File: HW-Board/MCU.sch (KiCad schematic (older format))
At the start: 22 parts

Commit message: sync
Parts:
- added C23, C24: 100n, symbol Device:C_Small
- added C25: 100n, symbol Device:C
- added J3: UART, symbol Connector:Conn_01x04_Male
- added R6, R7, R8: R, symbol Device:R
- added ROT1: ROTARY-ENCODER-Ebay, symbol Peters:ROTARY-ENCODER-Ebay
- added U8: SN74LVC2G14, TO_SOT_Packages_SMD:SOT-23-6_Handsoldering, symbol Peters:SN74LVC2G14
- gave numbers to parts that had none: 22
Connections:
- net +3V3: now also C25.1, R6.1, R7.1, R8.1, U8.5 (VCC)
- net GND: now also C23.2, C24.2, C25.2, J3.4 (Pin_4), ROT1.2 (C), ROT1.4 (SW2), U8.2 (GND)
- net RX: now also J3.3 (Pin_3)
- net TX: now also J3.2 (Pin_2)
- net encA: now reaches U6.15 (PB10_SCL2_TX3_5V)
- net encA: now also U8.6 (Y)
- net encSW: now reaches U6.16 (PB11_SDA2_RX3_5V)
- net encSW: now also R6.2, ROT1.5 (SW1)
- net NegativeSet1 renamed encB
- net encB: now also U8.4 (Y)
- net NegativeSet2: no longer names the net of U6.13 (PB0_ADC8_PWM)
- new net: C24.1, R7.2, ROT1.1 (A), U8.1 (A)
- new net: C23.1, R8.2, ROT1.3 (B), U8.3 (A)
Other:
- moved on the sheet: D2A, D3A, R_I2CPullUp1, R_I2CPullUp2

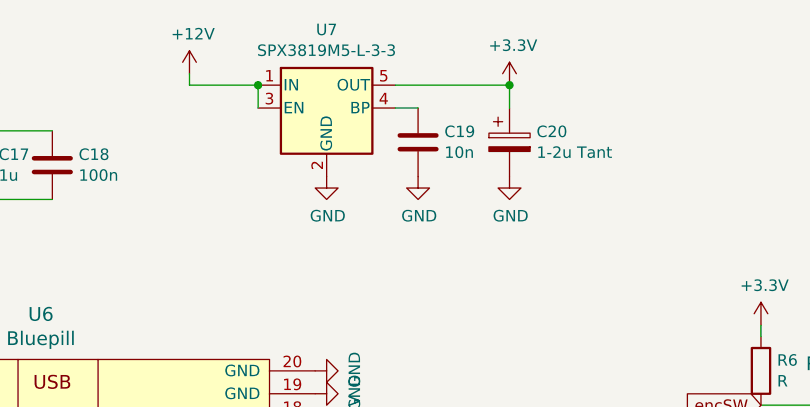
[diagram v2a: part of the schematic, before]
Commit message: 5v isolation and better opamps
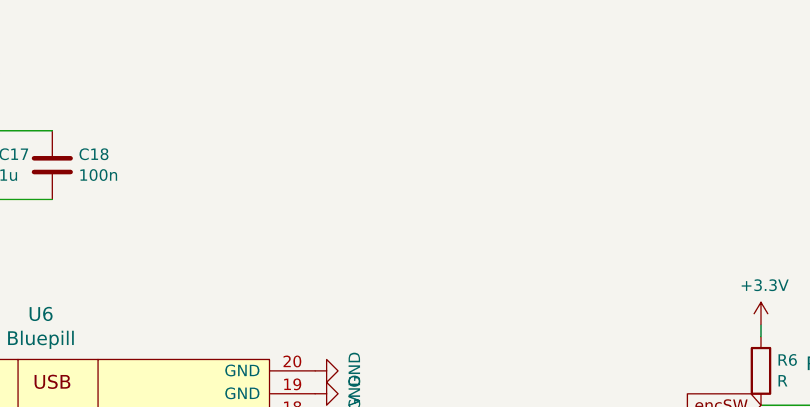
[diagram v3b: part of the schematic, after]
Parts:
- removed C19: 10n, symbol Device:C
- removed C20: 1-2u Tant, symbol Device:CP
- removed U7: SPX3819M5-L-3-3, Package_TO_SOT_SMD:SOT-23-5, symbol Regulator_Linear:SPX3819M5-L-3-3
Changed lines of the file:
@@
-$EndComp
-$Comp
-L Regulator_Linear:SPX3819M5-L-3-3 U7
-U 1 1 5D4D1C8C
-P 5100 1200
-F 0 "U7" H 5100 1542 50  0000 C CNN
-F 1 "SPX3819M5-L-3-3" H 5100 1451 50  0000 C CNN
-F 2 "Package_TO_SOT_SMD:SOT-23-5" H 5100 1525 50  0001 C CNN
-F 3 "https://www.exar.com/content/document.ashx?id=22106&languageid=1033&type=Datasheet&partnumber=SPX3819&filename=SPX3819.pdf&part=SPX3819" H 5100 1200 50  0001 C CNN
-	1    5100 1200
-	1    0    0    -1
-$EndComp
-$Comp
-L power:+12V #PWR0160
-U 1 1 5D4D49AD
-P 4500 1050
-F 0 "#PWR0160" H 4500 900 50  0001 C CNN
-F 1 "+12V" H 4515 1223 50  0000 C CNN
-F 2 "" H 4500 1050 50  0001 C CNN
-F 3 "" H 4500 1050 50  0001 C CNN
-	1    4500 1050
-	1    0    0    -1
-$EndComp
-Wire Wire Line
-	4800 1100 4500 1100
-Wire Wire Line
-	4500 1100 4500 1050
-$Comp
-L Device:C C?
-U 1 1 5D4D693C
-P 5500 1350
-AR Path="/5D4D693C" Ref="C?"  Part="1"
-AR Path="/5D42C521/5D4D693C" Ref="C19"  Part="1"
-F 0 "C19" H 5615 1396 50  0000 L CNN
-F 1 "10n" H 5615 1305 50  0000 L CNN
-F 2 "" H 5538 1200 50  0001 C CNN
-F 3 "~" H 5500 1350 50  0001 C CNN
-	1    5500 1350
-	1    0    0    -1
-$EndComp
-Wire Wire Line
-	5500 1200 5400 1200
-$Comp
-L power:+3.3V #PWR?
-U 1 1 5D4D890C
-P 5900 1100
-AR Path="/5D4D890C" Ref="#PWR?"  Part="1"
-AR Path="/5D42C521/5D4D890C" Ref="#PWR0162"  Part="1"
-F 0 "#PWR0162" H 5900 950 50  0001 C CNN
-F 1 "+3.3V" H 5915 1273 50  0000 C CNN
-F 2 "" H 5900 1100 50  0001 C CNN
-F 3 "" H 5900 1100 50  0001 C CNN
-	1    5900 1100
-	1    0    0    -1
-$EndComp
-Wire Wire Line
-	5400 1100 5900 1100
-Wire Wire Line
-	5900 1100 5900 1200
-Connection ~ 5900 1100
-Wire Wire Line
-	4800 1200 4800 1100
-Connection ~ 4800 1100
-$Comp
-L Device:CP C20
-U 1 1 5D4E21A7
-P 5900 1350
-F 0 "C20" H 6018 1396 50  0000 L CNN
-F 1 "1-2u Tant" H 6018 1305 50  0000 L CNN
-F 2 "" H 5938 1200 50  0001 C CNN
-F 3 "~" H 5900 1350 50  0001 C CNN
-	1    5900 1350
-	1    0    0    -1
 $EndComp
 $Comp
@@
 Text GLabel 1400 5900 2    50   Input ~ 0
 TX
-$Comp
-L power:GND #PWR?
-U 1 1 5D4DDDD2
-P 5900 1500
-AR Path="/5D4DDDD2" Ref="#PWR?"  Part="1"
-AR Path="/5D42C521/5D4DDDD2" Ref="#PWR0163"  Part="1"
-F 0 "#PWR0163" H 5900 1250 50  0001 C CNN
-F 1 "GND" H 5905 1327 50  0000 C CNN
-F 2 "" H 5900 1500 50  0001 C CNN
-F 3 "" H 5900 1500 50  0001 C CNN
-	1    5900 1500
-	1    0    0    -1
-$EndComp
-$Comp
-L power:GND #PWR?
-U 1 1 5D4D769E
-P 5500 1500
-AR Path="/5D4D769E" Ref="#PWR?"  Part="1"
-AR Path="/5D42C521/5D4D769E" Ref="#PWR0161"  Part="1"
-F 0 "#PWR0161" H 5500 1250 50  0001 C CNN
-F 1 "GND" H 5505 1327 50  0000 C CNN
-F 2 "" H 5500 1500 50  0001 C CNN
-F 3 "" H 5500 1500 50  0001 C CNN
-	1    5500 1500
-	1    0    0    -1
-$EndComp
-$Comp
-L power:GND #PWR?
-U 1 1 5D4D405D
-P 5100 1500
-AR Path="/5D4D405D" Ref="#PWR?"  Part="1"
-AR Path="/5D42C521/5D4D405D" Ref="#PWR0159"  Part="1"
-F 0 "#PWR0159" H 5100 1250 50  0001 C CNN
-F 1 "GND" H 5105 1327 50  0000 C CNN
-F 2 "" H 5100 1500 50  0001 C CNN
-F 3 "" H 5100 1500 50  0001 C CNN
-	1    5100 1500
-	1    0    0    -1
-$EndComp
 $EndSCHEMATC

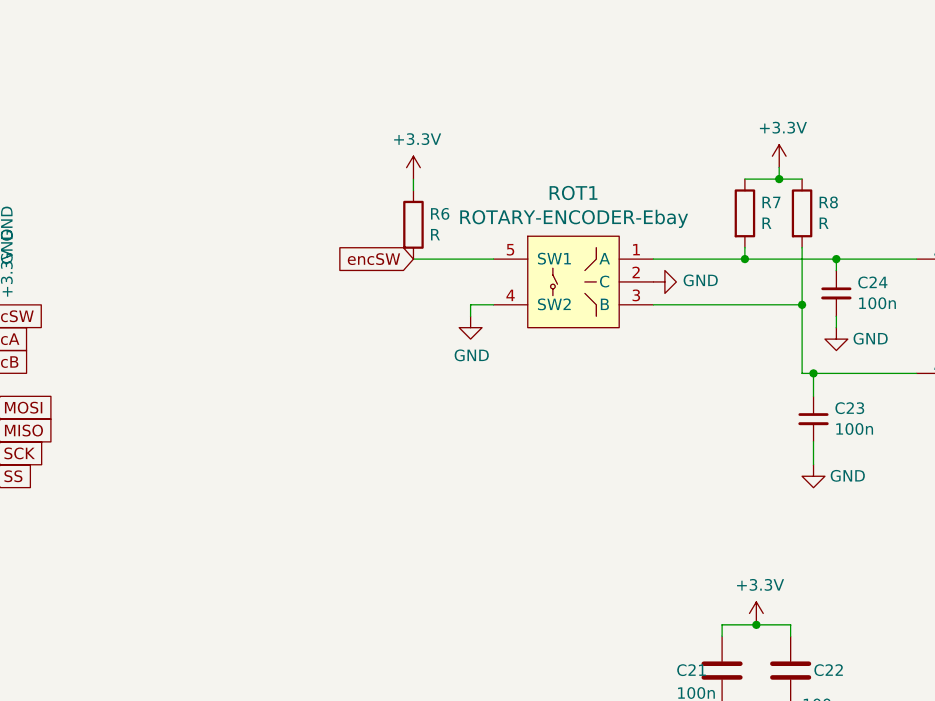
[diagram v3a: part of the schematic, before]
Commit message: added schmidt on encoder button
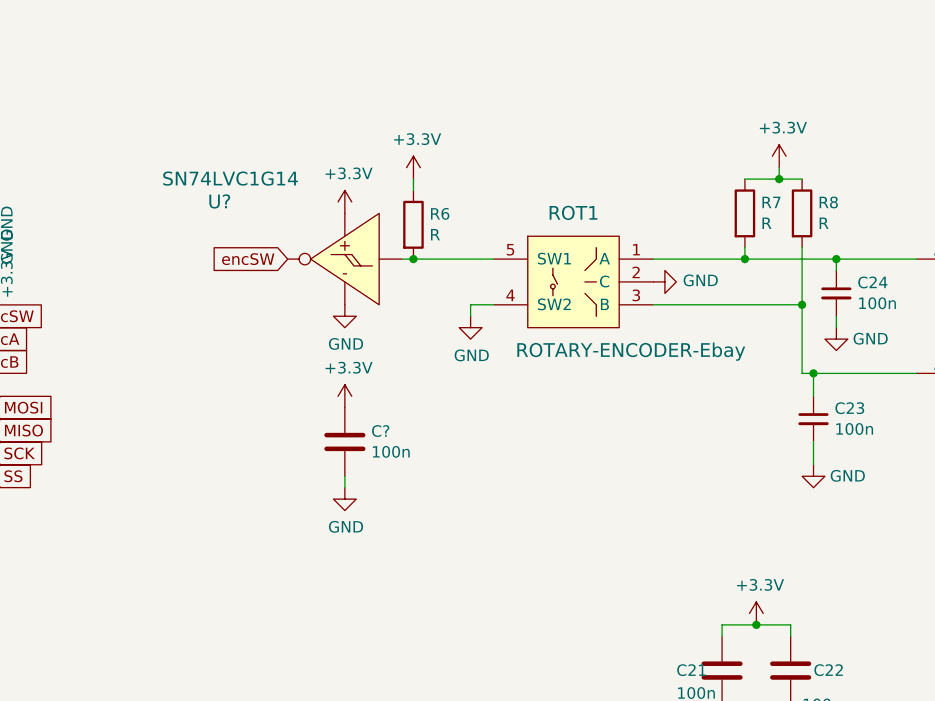
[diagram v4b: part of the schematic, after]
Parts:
- added C?: 100n, symbol Device:C
- added U?: SN74LVC1G14, TO_SOT_Packages_SMD:SOT-23-5_HandSoldering, symbol Peters:SN74LVC1G14
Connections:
- net +3V3: now also C?.1, U?.5 (VCC)
- net GND: now also C?.2, U?.3 (GND)
- net encSW: now also U?.4 (Y); no longer R6.2, ROT1.5 (SW1)
- new net: R6.2, ROT1.5 (SW1), U?.2 (A)
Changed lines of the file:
@@
 U 1 1 5D0958DD
 P 7700 2600
-F 0 "ROT1" H 7700 2987 60  0000 C CNN
-F 1 "ROTARY-ENCODER-Ebay" H 7700 2881 60  0000 C CNN
+F 0 "ROT1" H 7700 2900 60  0000 C CNN
+F 1 "ROTARY-ENCODER-Ebay" H 7950 2300 60  0000 C CNN
 F 2 "" H 7700 2600 60  0000 C CNN
 F 3 "" H 7700 2600 60  0000 C CNN
@@
 Text GLabel 9900 3000 2    50   Input ~ 0
 encB
-Text GLabel 7000 2500 0    50   Input ~ 0
+Text GLabel 6450 2500 0    50   Input ~ 0
 encSW
 Text GLabel 5050 2750 2    50   Input ~ 0
@@
 Text GLabel 1400 5900 2    50   Input ~ 0
 TX
+Wire Wire Line
+	7000 2500 6950 2500
+Connection ~ 7000 2500
+$Comp
+L Peters:SN74LVC1G14 U?
+U 1 1 5D50A9CE
+P 6700 2500
+F 0 "U?" H 7300 2750 60  0000 R CNN
+F 1 "SN74LVC1G14" H 7500 2850 60  0000 R CNN
+F 2 "TO_SOT_Packages_SMD:SOT-23-5_HandSoldering" H 6700 3250 60  0001 C CNN
+F 3 "" H 6700 3100 60  0001 C CNN
+	1    6700 2500
+	-1   0    0    -1
+$EndComp
+$Comp
+L power:+3.3V #PWR?
+U 1 1 5D523AB0
+P 6700 2300
+AR Path="/5D523AB0" Ref="#PWR?"  Part="1"
+AR Path="/5D42C521/5D523AB0" Ref="#PWR?"  Part="1"
+F 0 "#PWR?" H 6700 2150 50  0001 C CNN
+F 1 "+3.3V" H 6715 2473 50  0000 C CNN
+F 2 "" H 6700 2300 50  0001 C CNN
+F 3 "" H 6700 2300 50  0001 C CNN
+	1    6700 2300
+	1    0    0    -1
+$EndComp
+$Comp
+L power:GND #PWR?
+U 1 1 5D5241A7
+P 6700 2700
+F 0 "#PWR?" H 6700 2450 50  0001 C CNN
+F 1 "GND" H 6705 2527 50  0000 C CNN
+F 2 "" H 6700 2700 50  0001 C CNN
+F 3 "" H 6700 2700 50  0001 C CNN
+	1    6700 2700
+	1    0    0    -1
+$EndComp
+$Comp
+L Device:C C?
+U 1 1 5D524955
+P 6700 3300
+AR Path="/5D524955" Ref="C?"  Part="1"
+AR Path="/5D42C521/5D524955" Ref="C?"  Part="1"
+F 0 "C?" H 6815 3346 50  0000 L CNN
+F 1 "100n" H 6815 3255 50  0000 L CNN
+F 2 "" H 6738 3150 50  0001 C CNN
+F 3 "~" H 6700 3300 50  0001 C CNN
+	1    6700 3300
+	1    0    0    -1
+$EndComp
+$Comp
+L power:GND #PWR?
+U 1 1 5D52495F
+P 6700 3500
+AR Path="/5D52495F" Ref="#PWR?"  Part="1"
+AR Path="/5D42C521/5D52495F" Ref="#PWR?"  Part="1"
+F 0 "#PWR?" H 6700 3250 50  0001 C CNN
+F 1 "GND" H 6705 3327 50  0000 C CNN
+F 2 "" H 6700 3500 50  0001 C CNN
+F 3 "" H 6700 3500 50  0001 C CNN
+	1    6700 3500
+	1    0    0    -1
+$EndComp
+Wire Wire Line
+	6700 3450 6700 3500
+$Comp
+L power:+3.3V #PWR?
+U 1 1 5D52496A
+P 6700 3150
+AR Path="/5D52496A" Ref="#PWR?"  Part="1"
+AR Path="/5D42C521/5D52496A" Ref="#PWR?"  Part="1"
+F 0 "#PWR?" H 6700 3000 50  0001 C CNN
+F 1 "+3.3V" H 6715 3323 50  0000 C CNN
+F 2 "" H 6700 3150 50  0001 C CNN
+F 3 "" H 6700 3150 50  0001 C CNN
+	1    6700 3150
+	1    0    0    -1
+$EndComp
 $EndSCHEMATC

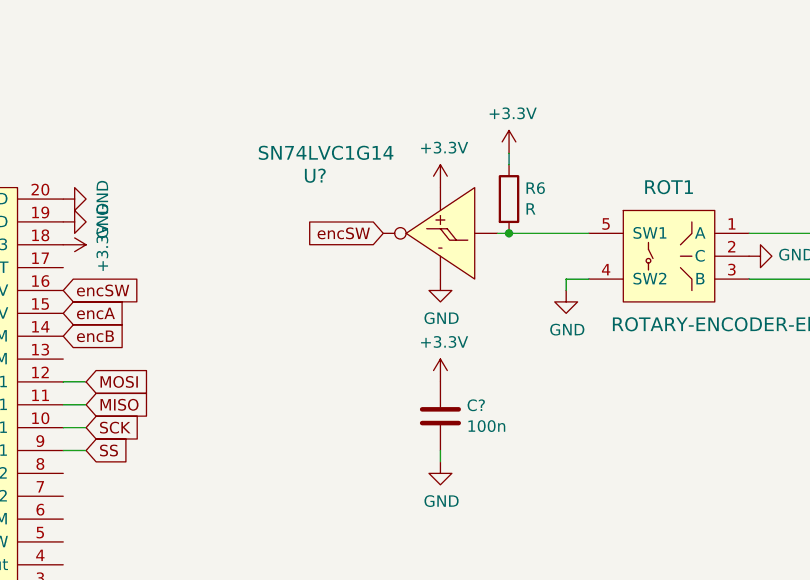
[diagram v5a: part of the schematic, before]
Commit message: Negative regulation done
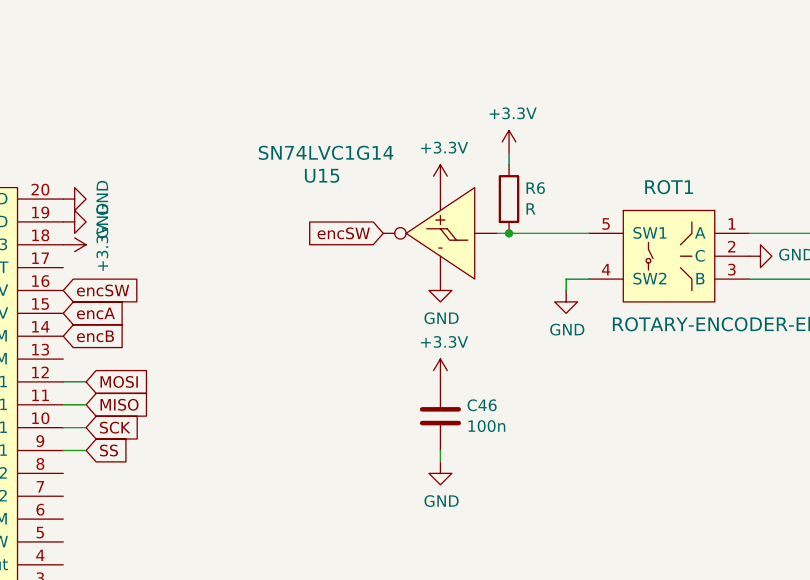
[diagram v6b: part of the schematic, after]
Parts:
- C15, C17, C18, C21, C22, C23, C24, C25: footprint (none) -> Capacitor_SMD:C_0805_2012Metric_Pad1.15x1.40mm_HandSolder
- C46: renamed from C?; footprint (none) -> Capacitor_SMD:C_0805_2012Metric_Pad1.15x1.40mm_HandSolder
- R4, R5, R6, R7, R8, R_I2CPullUp1, R_I2CPullUp2: footprint (none) -> Resistor_SMD:R_0805_2012Metric_Pad1.15x1.40mm_HandSolder
- ROT1: footprint (none) -> Libs:ROTARY-ENCODER-Ebay
- gave numbers to parts that had none: 1
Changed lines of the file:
@@
 EESchema Schematic File Version 4
 LIBS:BreadbaordPSU-cache
-EELAYER 29 0
+EELAYER 30 0
 EELAYER END
 $Descr A4 11693 8268
@@
 Sheet 3 4
 Title "Isolated adjustible +/- VDC PSU"
-Date ""
+Date "2019-09-03"
 Rev ""
 Comp ""
@@
 F 0 "R5" V 2350 2950 50  0000 L CNN
 F 1 "1K" V 2450 2900 50  0000 L CNN
-F 2 "" V 2380 2950 50  0001 C CNN
+F 2 "Resistor_SMD:R_0805_2012Metric_Pad1.15x1.40mm_HandSolder" V 2380 2950 50  0001 C CNN
 F 3 "~" H 2450 2950 50  0001 C CNN
 	1    2450 2950
@@
 F 0 "C15" H 3165 4846 50  0000 L CNN
 F 1 "100n" H 3165 4755 50  0000 L CNN
-F 2 "" H 3088 4650 50  0001 C CNN
+F 2 "Capacitor_SMD:C_0805_2012Metric_Pad1.15x1.40mm_HandSolder" H 3088 4650 50  0001 C CNN
 F 3 "~" H 3050 4800 50  0001 C CNN
 	1    3050 4800
@@
 F 0 "C17" H 3665 1496 50  0000 L CNN
 F 1 "1u" H 3665 1405 50  0000 L CNN
-F 2 "" H 3588 1300 50  0001 C CNN
+F 2 "Capacitor_SMD:C_0805_2012Metric_Pad1.15x1.40mm_HandSolder" H 3588 1300 50  0001 C CNN
 F 3 "~" H 3550 1450 50  0001 C CNN
 	1    3550 1450
@@
 F 0 "C18" H 4015 1496 50  0000 L CNN
 F 1 "100n" H 4015 1405 50  0000 L CNN
-F 2 "" H 3938 1300 50  0001 C CNN
+F 2 "Capacitor_SMD:C_0805_2012Metric_Pad1.15x1.40mm_HandSolder" H 3938 1300 50  0001 C CNN
 F 3 "~" H 3900 1450 50  0001 C CNN
 	1    3900 1450
@@
 F 0 "R_I2CPullUp1" V 2400 1100 50  0000 L CNN
 F 1 "1K" V 2550 1350 50  0000 L CNN
-F 2 "" V 2480 1400 50  0001 C CNN
+F 2 "Resistor_SMD:R_0805_2012Metric_Pad1.15x1.40mm_HandSolder" V 2480 1400 50  0001 C CNN
 F 3 "~" H 2550 1400 50  0001 C CNN
 	1    2550 1400
@@
 F 0 "R_I2CPullUp2" V 2850 1050 50  0000 L CNN
 F 1 "1K" V 2750 1350 50  0000 L CNN
-F 2 "" V 2680 1400 50  0001 C CNN
+F 2 "Resistor_SMD:R_0805_2012Metric_Pad1.15x1.40mm_HandSolder" V 2680 1400 50  0001 C CNN
 F 3 "~" H 2750 1400 50  0001 C CNN
 	1    2750 1400
@@
 F 0 "C21" H 8150 4300 50  0000 L CNN
 F 1 "100n" H 8150 4200 50  0000 L CNN
-F 2 "" H 8388 4150 50  0001 C CNN
+F 2 "Capacitor_SMD:C_0805_2012Metric_Pad1.15x1.40mm_HandSolder" H 8388 4150 50  0001 C CNN
 F 3 "~" H 8350 4300 50  0001 C CNN
 	1    8350 4300
@@
 F 0 "C22" H 8750 4300 50  0000 L CNN
 F 1 "100n" H 8700 4150 50  0000 L CNN
-F 2 "" H 8688 4150 50  0001 C CNN
+F 2 "Capacitor_SMD:C_0805_2012Metric_Pad1.15x1.40mm_HandSolder" H 8688 4150 50  0001 C CNN
 F 3 "~" H 8650 4300 50  0001 C CNN
 	1    8650 4300
@@
 F 0 "R4" V 2550 3000 50  0000 L CNN
 F 1 "1K" V 2450 2800 50  0000 L CNN
-F 2 "" V 2380 2850 50  0001 C CNN
+F 2 "Resistor_SMD:R_0805_2012Metric_Pad1.15x1.40mm_HandSolder" V 2380 2850 50  0001 C CNN
 F 3 "~" H 2450 2850 50  0001 C CNN
 	1    2450 2850
@@
 F 0 "ROT1" H 7700 2900 60  0000 C CNN
 F 1 "ROTARY-ENCODER-Ebay" H 7950 2300 60  0000 C CNN
-F 2 "" H 7700 2600 60  0000 C CNN
+F 2 "Libs:ROTARY-ENCODER-Ebay" H 7700 2600 60  0001 C CNN
 F 3 "" H 7700 2600 60  0000 C CNN
 	1    7700 2600
@@
 F 0 "R6" H 7070 2396 50  0000 L CNN
 F 1 "R" H 7070 2305 50  0000 L CNN
-F 2 "" V 6930 2350 50  0001 C CNN
+F 2 "Resistor_SMD:R_0805_2012Metric_Pad1.15x1.40mm_HandSolder" V 6930 2350 50  0001 C CNN
 F 3 "~" H 7000 2350 50  0001 C CNN
 	1    7000 2350
@@
 F 0 "R7" H 8520 2346 50  0000 L CNN
 F 1 "R" H 8520 2255 50  0000 L CNN
-F 2 "" V 8380 2300 50  0001 C CNN
+F 2 "Resistor_SMD:R_0805_2012Metric_Pad1.15x1.40mm_HandSolder" V 8380 2300 50  0001 C CNN
 F 3 "~" H 8450 2300 50  0001 C CNN
 	1    8450 2300
@@
 F 0 "R8" H 8770 2346 50  0000 L CNN
 F 1 "R" H 8770 2255 50  0000 L CNN
-F 2 "" V 8630 2300 50  0001 C CNN
+F 2 "Resistor_SMD:R_0805_2012Metric_Pad1.15x1.40mm_HandSolder" V 8630 2300 50  0001 C CNN
 F 3 "~" H 8700 2300 50  0001 C CNN
 	1    8700 2300
@@
 F 0 "C24" H 8942 2696 50  0000 L CNN
 F 1 "100n" H 8942 2605 50  0000 L CNN
-F 2 "" H 8850 2650 50  0001 C CNN
+F 2 "Capacitor_SMD:C_0805_2012Metric_Pad1.15x1.40mm_HandSolder" H 8850 2650 50  0001 C CNN
 F 3 "~" H 8850 2650 50  0001 C CNN
 	1    8850 2650
@@
 F 0 "C23" H 8842 3246 50  0000 L CNN
 F 1 "100n" H 8842 3155 50  0000 L CNN
-F 2 "" H 8750 3200 50  0001 C CNN
+F 2 "Capacitor_SMD:C_0805_2012Metric_Pad1.15x1.40mm_HandSolder" H 8750 3200 50  0001 C CNN
 F 3 "~" H 8750 3200 50  0001 C CNN
 	1    8750 3200
@@
 F 0 "C25" H 9865 1646 50  0000 L CNN
 F 1 "100n" H 9865 1555 50  0000 L CNN
-F 2 "" H 9788 1450 50  0001 C CNN
+F 2 "Capacitor_SMD:C_0805_2012Metric_Pad1.15x1.40mm_HandSolder" H 9788 1450 50  0001 C CNN
 F 3 "~" H 9750 1600 50  0001 C CNN
 	1    9750 1600
@@
 Connection ~ 7000 2500
 $Comp
-L Peters:SN74LVC1G14 U?
+L Peters:SN74LVC1G14 U15
 U 1 1 5D50A9CE
 P 6700 2500
-F 0 "U?" H 7300 2750 60  0000 R CNN
+F 0 "U15" H 7300 2750 60  0000 R CNN
 F 1 "SN74LVC1G14" H 7500 2850 60  0000 R CNN
 F 2 "TO_SOT_Packages_SMD:SOT-23-5_HandSoldering" H 6700 3250 60  0001 C CNN
@@
 P 6700 2300
 AR Path="/5D523AB0" Ref="#PWR?"  Part="1"
-AR Path="/5D42C521/5D523AB0" Ref="#PWR?"  Part="1"
-F 0 "#PWR?" H 6700 2150 50  0001 C CNN
+AR Path="/5D42C521/5D523AB0" Ref="#PWR0229"  Part="1"
+F 0 "#PWR0229" H 6700 2150 50  0001 C CNN
 F 1 "+3.3V" H 6715 2473 50  0000 C CNN
 F 2 "" H 6700 2300 50  0001 C CNN
@@
 $EndComp
 $Comp
-L power:GND #PWR?
+L power:GND #PWR0230
 U 1 1 5D5241A7
 P 6700 2700
-F 0 "#PWR?" H 6700 2450 50  0001 C CNN
+F 0 "#PWR0230" H 6700 2450 50  0001 C CNN
 F 1 "GND" H 6705 2527 50  0000 C CNN
 F 2 "" H 6700 2700 50  0001 C CNN
@@
 P 6700 3300
 AR Path="/5D524955" Ref="C?"  Part="1"
-AR Path="/5D42C521/5D524955" Ref="C?"  Part="1"
-F 0 "C?" H 6815 3346 50  0000 L CNN
+AR Path="/5D42C521/5D524955" Ref="C46"  Part="1"
+F 0 "C46" H 6815 3346 50  0000 L CNN
 F 1 "100n" H 6815 3255 50  0000 L CNN
-F 2 "" H 6738 3150 50  0001 C CNN
+F 2 "Capacitor_SMD:C_0805_2012Metric_Pad1.15x1.40mm_HandSolder" H 6738 3150 50  0001 C CNN
 F 3 "~" H 6700 3300 50  0001 C CNN
 	1    6700 3300
@@
 P 6700 3500
 AR Path="/5D52495F" Ref="#PWR?"  Part="1"
-AR Path="/5D42C521/5D52495F" Ref="#PWR?"  Part="1"
-F 0 "#PWR?" H 6700 3250 50  0001 C CNN
+AR Path="/5D42C521/5D52495F" Ref="#PWR0231"  Part="1"
+F 0 "#PWR0231" H 6700 3250 50  0001 C CNN
 F 1 "GND" H 6705 3327 50  0000 C CNN
 F 2 "" H 6700 3500 50  0001 C CNN
@@
 P 6700 3150
 AR Path="/5D52496A" Ref="#PWR?"  Part="1"
-AR Path="/5D42C521/5D52496A" Ref="#PWR?"  Part="1"
-F 0 "#PWR?" H 6700 3000 50  0001 C CNN
+AR Path="/5D42C521/5D52496A" Ref="#PWR0232"  Part="1"
+F 0 "#PWR0232" H 6700 3000 50  0001 C CNN
 F 1 "+3.3V" H 6715 3323 50  0000 C CNN
 F 2 "" H 6700 3150 50  0001 C CNN

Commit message: PDF sync
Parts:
- J3: footprint (none) -> Connector_PinSocket_2.54mm:PinSocket_1x04_P2.54mm_Vertical
- JP2: footprint (none) -> Jumper:SolderJumper-3_P1.3mm_Bridged2Bar12_Pad1.0x1.5mm
- TP1, TP2, TP3, TP4: footprint (none) -> TestPoint:TestPoint_Pad_D1.0mm
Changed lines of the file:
@@
 F 0 "JP2" V 8046 5718 50  0000 L CNN
 F 1 "EXTMODE" H 7950 5900 50  0000 L CNN
-F 2 "" H 8000 5650 50  0001 C CNN
+F 2 "Jumper:SolderJumper-3_P1.3mm_Bridged2Bar12_Pad1.0x1.5mm" H 8000 5650 50  0001 C CNN
 F 3 "~" H 8000 5650 50  0001 C CNN
 	1    8000 5650
@@
 F 0 "TP1" V 6250 5950 50  0000 L CNN
 F 1 "MOSI_TP" V 6150 6100 50  0000 L CNN
-F 2 "" H 6350 5900 50  0001 C CNN
+F 2 "TestPoint:TestPoint_Pad_D1.0mm" H 6350 5900 50  0001 C CNN
 F 3 "~" H 6350 5900 50  0001 C CNN
 	1    6150 5900
@@
 F 0 "TP2" V 6450 5950 50  0000 L CNN
 F 1 "MISO_TP" V 6350 6100 50  0000 L CNN
-F 2 "" H 6550 5900 50  0001 C CNN
+F 2 "TestPoint:TestPoint_Pad_D1.0mm" H 6550 5900 50  0001 C CNN
 F 3 "~" H 6550 5900 50  0001 C CNN
 	1    6350 5900
@@
 F 0 "TP3" V 6650 5950 50  0000 L CNN
 F 1 "SCK_TP" V 6550 6100 50  0000 L CNN
-F 2 "" H 6750 5900 50  0001 C CNN
+F 2 "TestPoint:TestPoint_Pad_D1.0mm" H 6750 5900 50  0001 C CNN
 F 3 "~" H 6750 5900 50  0001 C CNN
 	1    6550 5900
@@
 F 0 "TP4" V 6850 5950 50  0000 L CNN
 F 1 "SS_TP" V 6750 6100 50  0000 L CNN
-F 2 "" H 6950 5900 50  0001 C CNN
+F 2 "TestPoint:TestPoint_Pad_D1.0mm" H 6950 5900 50  0001 C CNN
 F 3 "~" H 6950 5900 50  0001 C CNN
 	1    6750 5900
@@
 F 0 "J3" H 1308 6181 50  0000 C CNN
 F 1 "UART" H 1308 6090 50  0000 C CNN
-F 2 "" H 1200 5900 50  0001 C CNN
+F 2 "Connector_PinSocket_2.54mm:PinSocket_1x04_P2.54mm_Vertical" H 1200 5900 50  0001 C CNN
 F 3 "~" H 1200 5900 50  0001 C CNN
 	1    1200 5900
